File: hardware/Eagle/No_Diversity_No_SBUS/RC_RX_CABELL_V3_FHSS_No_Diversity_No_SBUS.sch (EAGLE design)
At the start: 22 parts, among them IC1 AMS1117 3V3, M1 NRF24L01, M2 NRF24L01

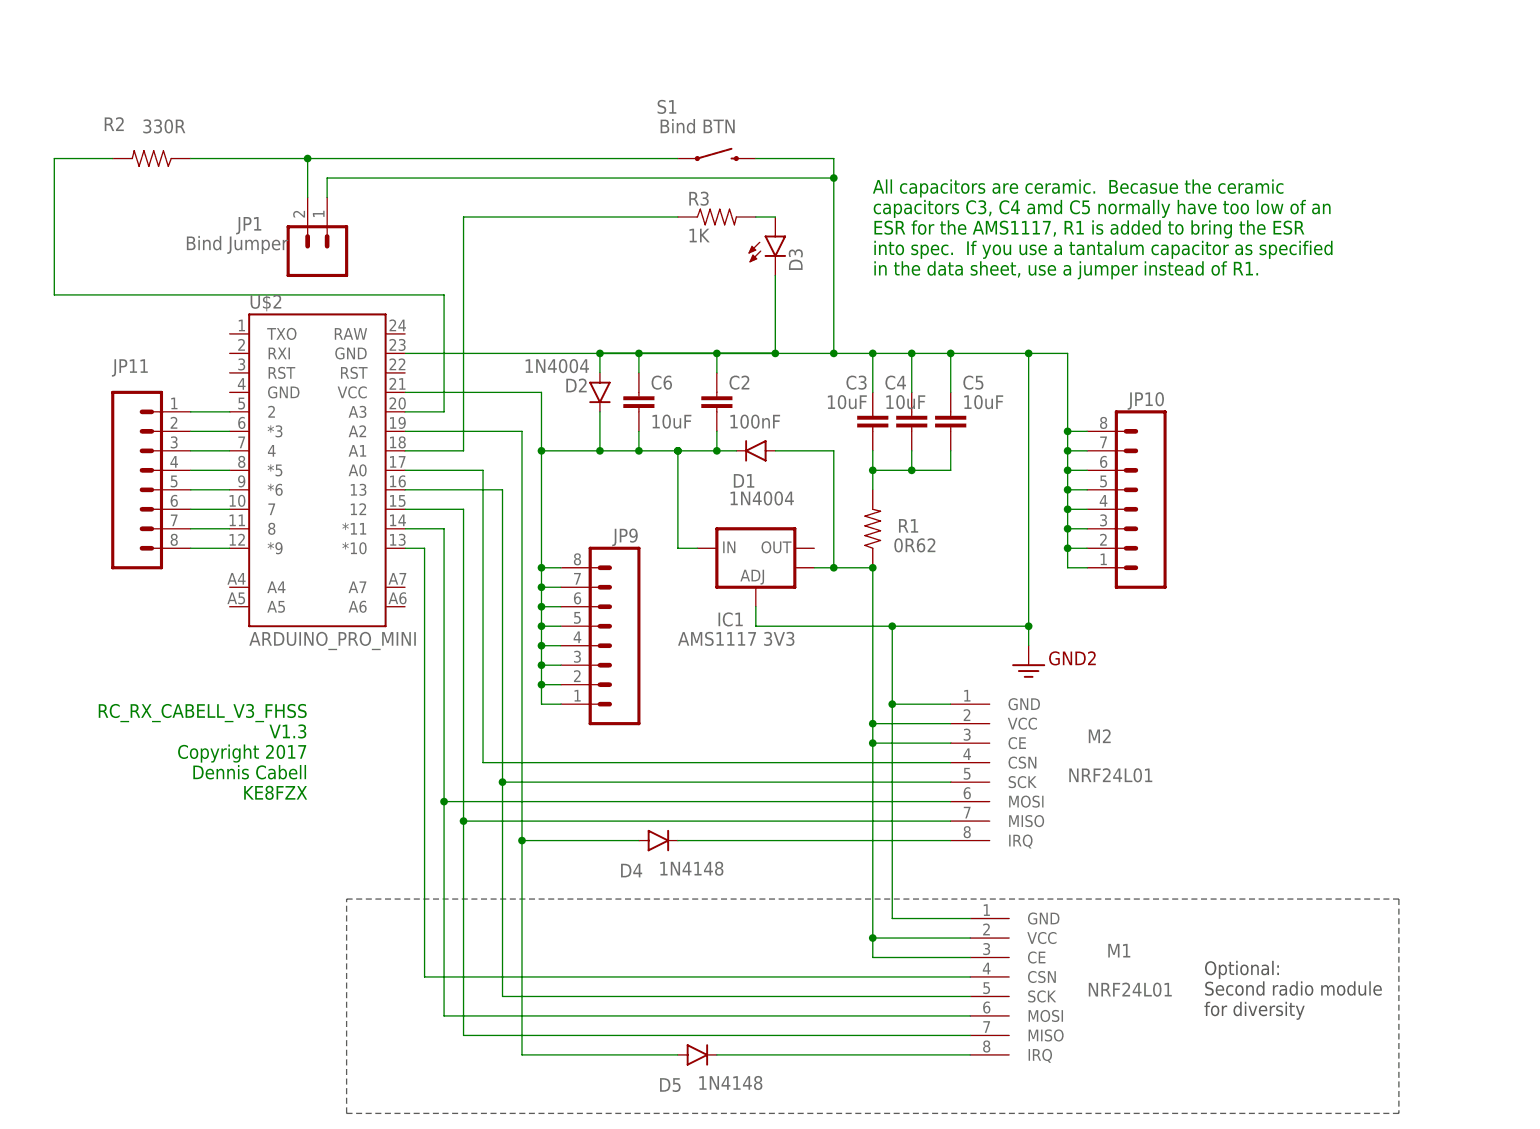
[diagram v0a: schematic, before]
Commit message: Hardware Updates for SBUS & PPM
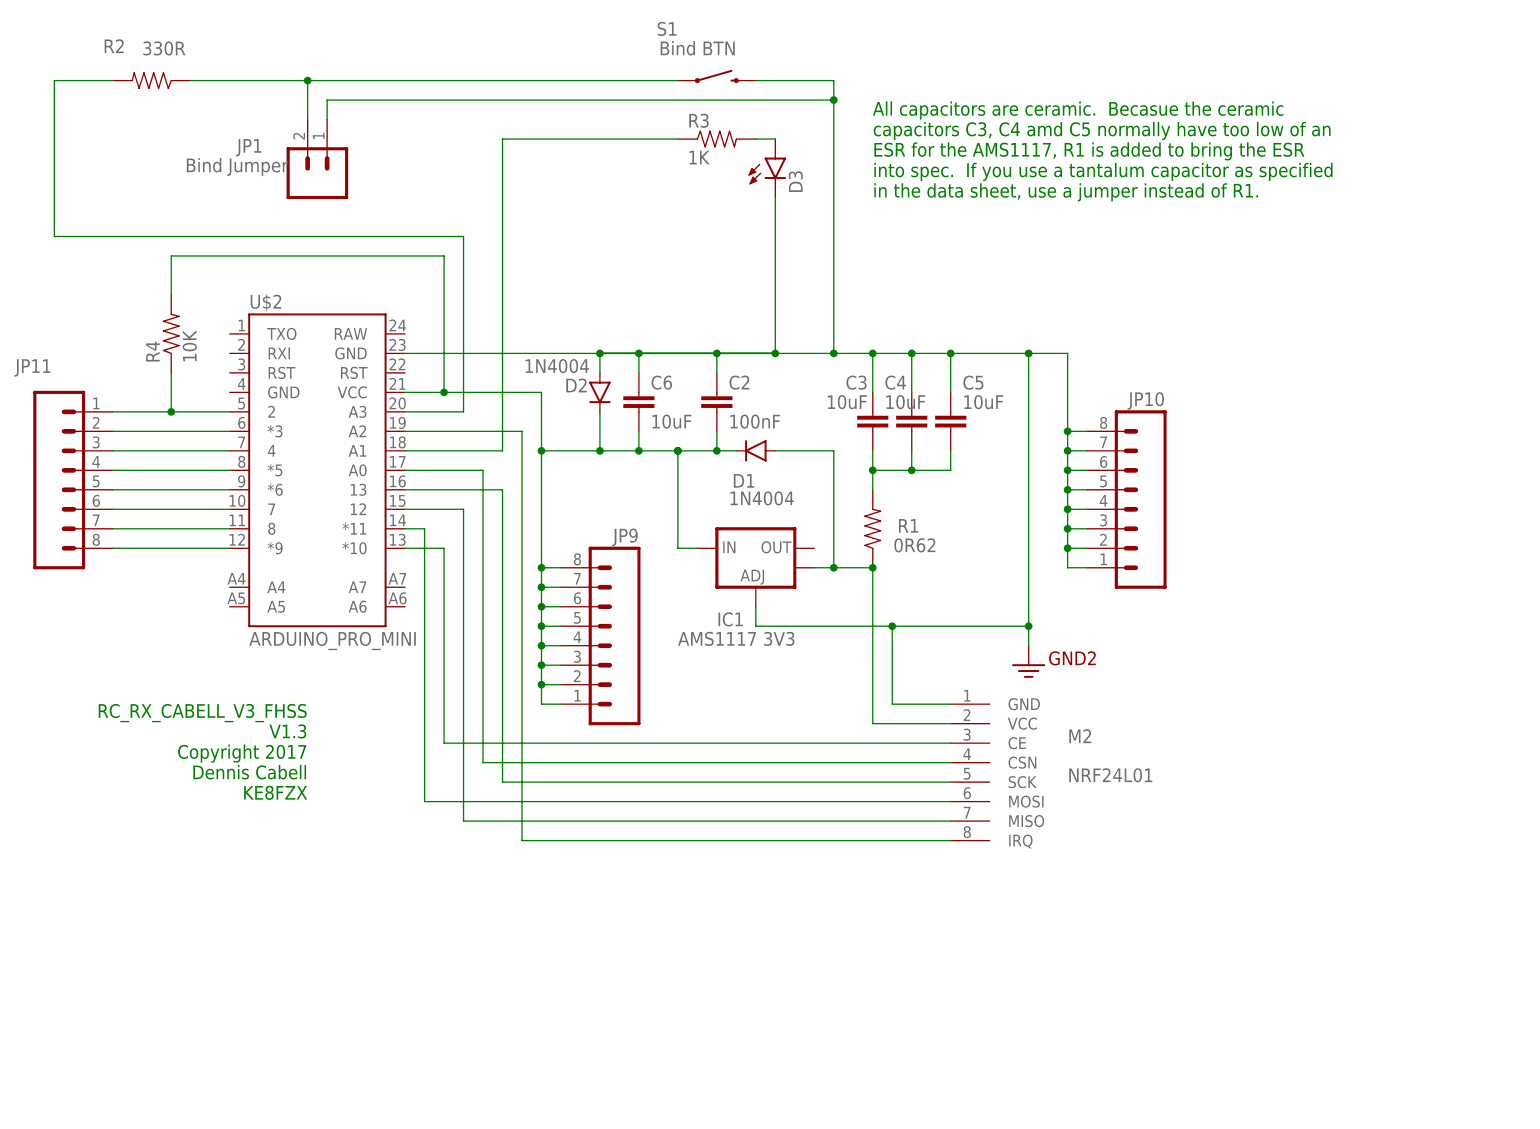
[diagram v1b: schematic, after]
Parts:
- removed D4: 1N4148, SparkFun-DiscreteSemi:DIODE1N4148
- removed D5: 1N4148, SparkFun-DiscreteSemi:DIODEPTH
- removed M1: NRF24L01, diy-modules:WIRELESS-NRF24L01
- added R4: 10K, SparkFun-Passives:RESISTORAXIAL-0.3
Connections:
- removed net N$16: D4.C, M2.IRQ
- removed net N$17: D5.C, M1.IRQ
- removed net N$23: M1.CSN, U$2.*10
- new net N$3: M2.CE, U$2.*10
- net 5V: now also R4.2
- net GND: no longer M1.GND
- net N$1: now also R4.1
- net N$13: now also M2.IRQ; no longer D4.A, D5.A
- net N$15: no longer M1.SCK
- net N$20: no longer M1.MOSI
- net N$22: no longer M1.MISO
- net VCC: no longer M1.CE, M1.VCC, M2.CE
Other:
- note removed: "Optional: Second radio module for diversity"
- moved on the sheet: D3, JP1, JP11, R2, R3, S1
